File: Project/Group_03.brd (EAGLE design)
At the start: 56.4 x 71.1 mm, 29 parts, among them J1 POWER_JACKPTH_LOCK, U1 +12v, U3 TCA9546APW, U4 TMUX1208RSV

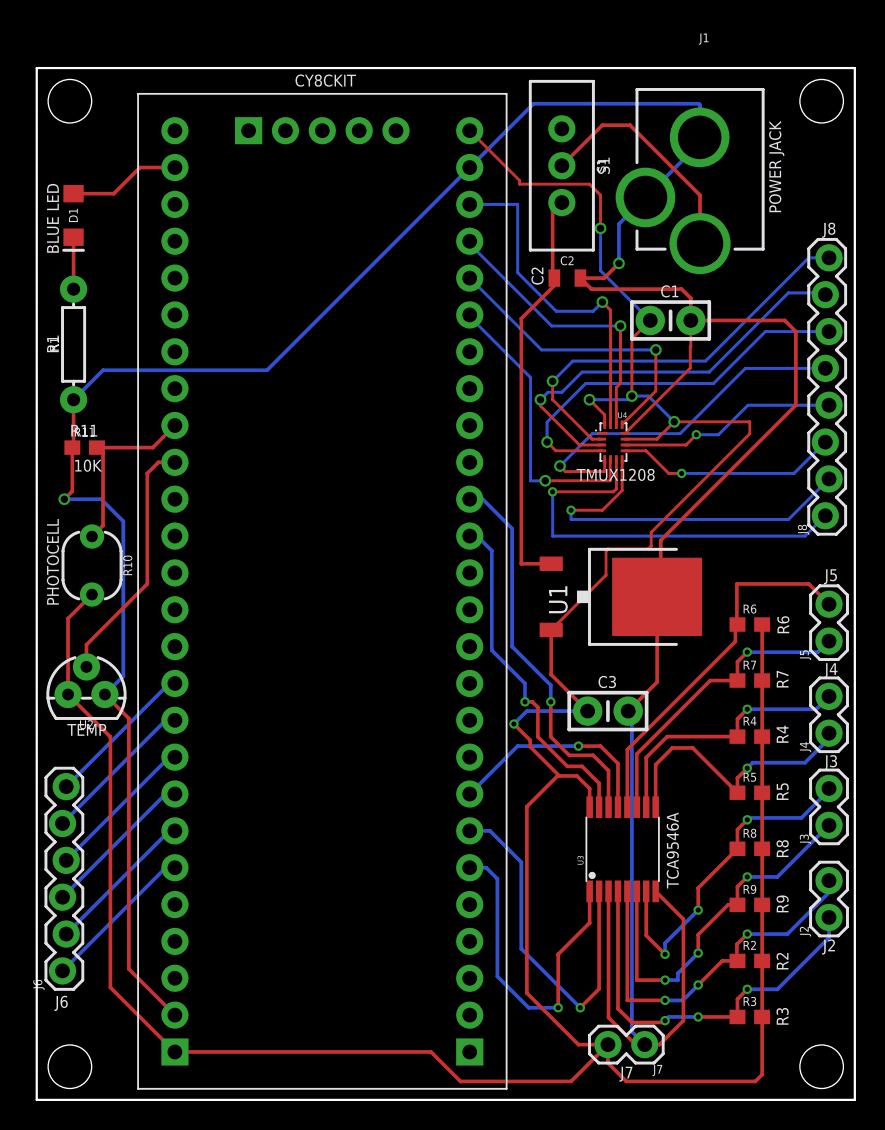
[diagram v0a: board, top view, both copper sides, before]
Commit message: Change silkscreen line width in Library for MUX, TCA and CY8
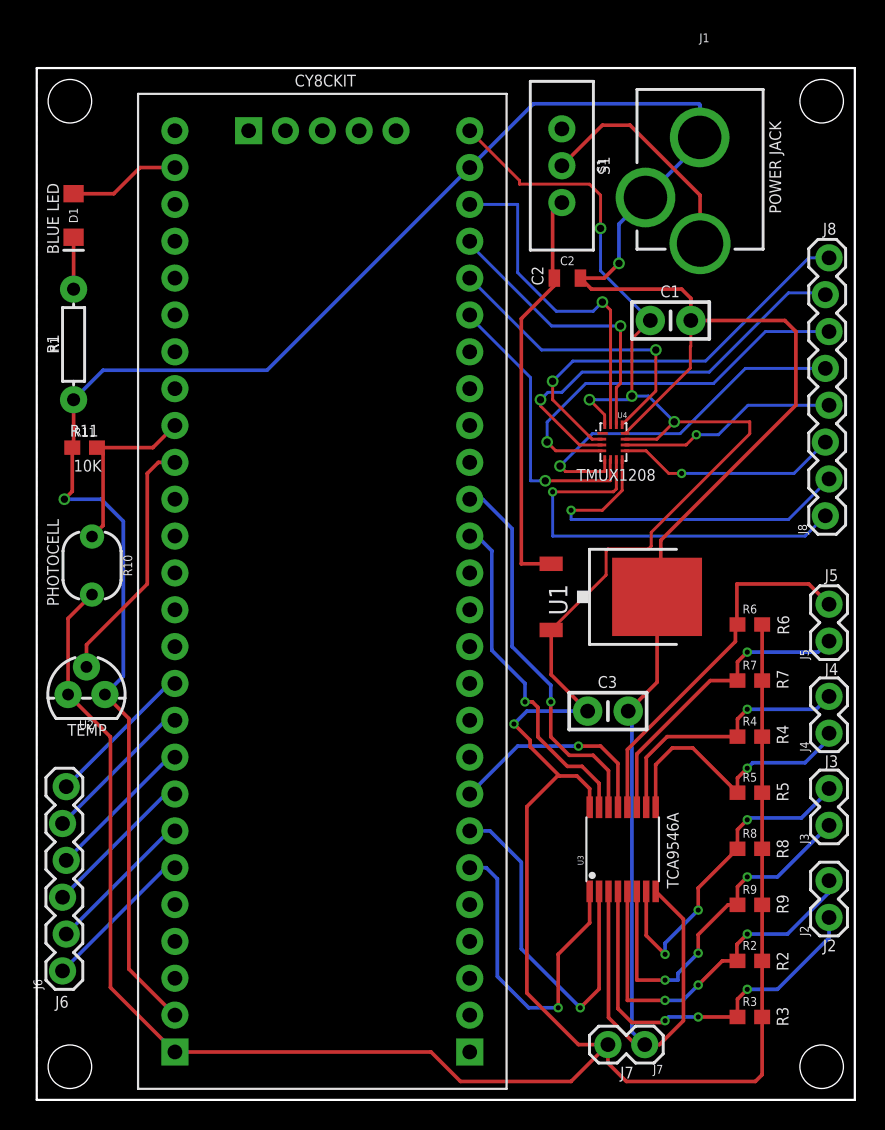
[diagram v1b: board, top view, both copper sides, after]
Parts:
- U$1: device CY8KIT-059:CY8CKIT-059_TARGET -> Group_03_Library:CY8CKIT-059_TARGET
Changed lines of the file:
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@@
 <layers>
 <layer number="1" name="Top" color="4" fill="1" visible="yes" active="yes"/>
-<layer number="16" name="Bottom" color="1" fill="1" visible="yes" active="yes"/>
-<layer number="17" name="Pads" color="2" fill="1" visible="yes" active="yes"/>
-<layer number="18" name="Vias" color="2" fill="1" visible="yes" active="yes"/>
-<layer number="19" name="Unrouted" color="6" fill="1" visible="yes" active="yes"/>
-<layer number="20" name="Dimension" color="61" fill="1" visible="yes" active="yes"/>
+<layer number="16" name="Bottom" color="1" fill="1" visible="no" active="yes"/>
+<layer number="17" name="Pads" color="2" fill="1" visible="no" active="yes"/>
+<layer number="18" name="Vias" color="2" fill="1" visible="no" active="yes"/>
+<layer number="19" name="Unrouted" color="6" fill="1" visible="no" active="yes"/>
+<layer number="20" name="Dimension" color="61" fill="1" visible="no" active="yes"/>
 <layer number="21" name="tPlace" color="13" fill="1" visible="yes" active="yes"/>
-<layer number="22" name="bPlace" color="7" fill="1" visible="yes" active="yes"/>
-<layer number="23" name="tOrigins" color="15" fill="1" visible="yes" active="yes"/>
-<layer number="24" name="bOrigins" color="15" fill="1" visible="yes" active="yes"/>
-<layer number="25" name="tNames" color="7" fill="1" visible="yes" active="yes"/>
-<layer number="26" name="bNames" color="7" fill="1" visible="yes" active="yes"/>
-<layer number="27" name="tValues" color="7" fill="1" visible="yes" active="yes"/>
-<layer number="28" name="bValues" color="7" fill="1" visible="yes" active="yes"/>
+<layer number="22" name="bPlace" color="7" fill="1" visible="no" active="yes"/>
+<layer number="23" name="tOrigins" color="15" fill="1" visible="no" active="yes"/>
+<layer number="24" name="bOrigins" color="15" fill="1" visible="no" active="yes"/>
+<layer number="25" name="tNames" color="7" fill="1" visible="no" active="yes"/>
+<layer number="26" name="bNames" color="7" fill="1" visible="no" active="yes"/>
+<layer number="27" name="tValues" color="7" fill="1" visible="no" active="yes"/>
+<layer number="28" name="bValues" color="7" fill="1" visible="no" active="yes"/>
 <layer number="29" name="tStop" color="7" fill="3" visible="no" active="yes"/>
 <layer number="30" name="bStop" color="7" fill="6" visible="no" active="yes"/>
@@
 <layer number="33" name="tFinish" color="6" fill="3" visible="no" active="yes"/>
 <layer number="34" name="bFinish" color="6" fill="6" visible="no" active="yes"/>
-<layer number="35" name="tGlue" color="7" fill="4" visible="yes" active="yes"/>
+<layer number="35" name="tGlue" color="7" fill="4" visible="no" active="yes"/>
 <layer number="36" name="bGlue" color="7" fill="5" visible="no" active="yes"/>
-<layer number="37" name="tTest" color="7" fill="1" visible="yes" active="yes"/>
-<layer number="38" name="bTest" color="7" fill="1" visible="yes" active="yes"/>
-<layer number="39" name="tKeepout" color="4" fill="11" visible="yes" active="yes"/>
-<layer number="40" name="bKeepout" color="1" fill="11" visible="yes" active="yes"/>
+<layer number="37" name="tTest" color="7" fill="1" visible="no" active="yes"/>
+<layer number="38" name="bTest" color="7" fill="1" visible="no" active="yes"/>
+<layer number="39" name="tKeepout" color="4" fill="11" visible="no" active="yes"/>
+<layer number="40" name="bKeepout" color="1" fill="11" visible="no" active="yes"/>
 <layer number="41" name="tRestrict" color="4" fill="10" visible="no" active="yes"/>
 <layer number="42" name="bRestrict" color="1" fill="10" visible="no" active="yes"/>
 <layer number="43" name="vRestrict" color="2" fill="10" visible="no" active="yes"/>
 <layer number="44" name="Drills" color="7" fill="1" visible="no" active="yes"/>
-<layer number="45" name="Holes" color="63" fill="1" visible="yes" active="yes"/>
+<layer number="45" name="Holes" color="63" fill="1" visible="no" active="yes"/>
 <layer number="46" name="Milling" color="3" fill="1" visible="no" active="yes"/>
 <layer number="47" name="Measures" color="7" fill="1" visible="no" active="yes"/>
-<layer number="48" name="Document" color="7" fill="1" visible="yes" active="yes"/>
-<layer number="49" name="Reference" color="7" fill="1" visible="yes" active="yes"/>
+<layer number="48" name="Document" color="7" fill="1" visible="no" active="yes"/>
+<layer number="49" name="Reference" color="7" fill="1" visible="no" active="yes"/>
 <layer number="50" name="dxf" color="7" fill="1" visible="no" active="no"/>
-<layer number="51" name="tDocu" color="7" fill="1" visible="yes" active="yes"/>
-<layer number="52" name="bDocu" color="7" fill="1" visible="yes" active="yes"/>
+<layer number="51" name="tDocu" color="7" fill="1" visible="no" active="yes"/>
+<layer number="52" name="bDocu" color="7" fill="1" visible="no" active="yes"/>
 <layer number="53" name="tGND_GNDA" color="7" fill="9" visible="no" active="no"/>
 <layer number="54" name="bGND_GNDA" color="1" fill="9" visible="no" active="no"/>
@@
 <attribute name="VALUE" x="33.782" y="64.389" size="0.6096" layer="27" font="vector" ratio="20" rot="R270" align="top-center"/>
 </element>
-<element name="U$1" library="CY8KIT-059" package="CY8CKIT-059_TARGET" value="CY8CKIT-059_TARGET" x="20.955" y="33.782" smashed="yes" rot="R270"/>
+<element name="U$1" library="Group_03_Library" package="CY8CKIT-059_TARGET" value="CY8CKIT-059_TARGET" x="20.955" y="33.782" smashed="yes" rot="R270"/>
 <element name="U1" library="SparkFun-IC-Power" package="TO-252" value="+12v" x="40.259" y="34.671" smashed="yes" rot="R270">
 <attribute name="NAME" x="36.576" y="33.401" size="1.27" layer="25" rot="R90"/>

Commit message: Last modifications to schematic, board and check rules
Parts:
- R1: value (none) -> 330
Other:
- board text added: "CY8CKIT-059"
- board text removed: "CY8CKIT"

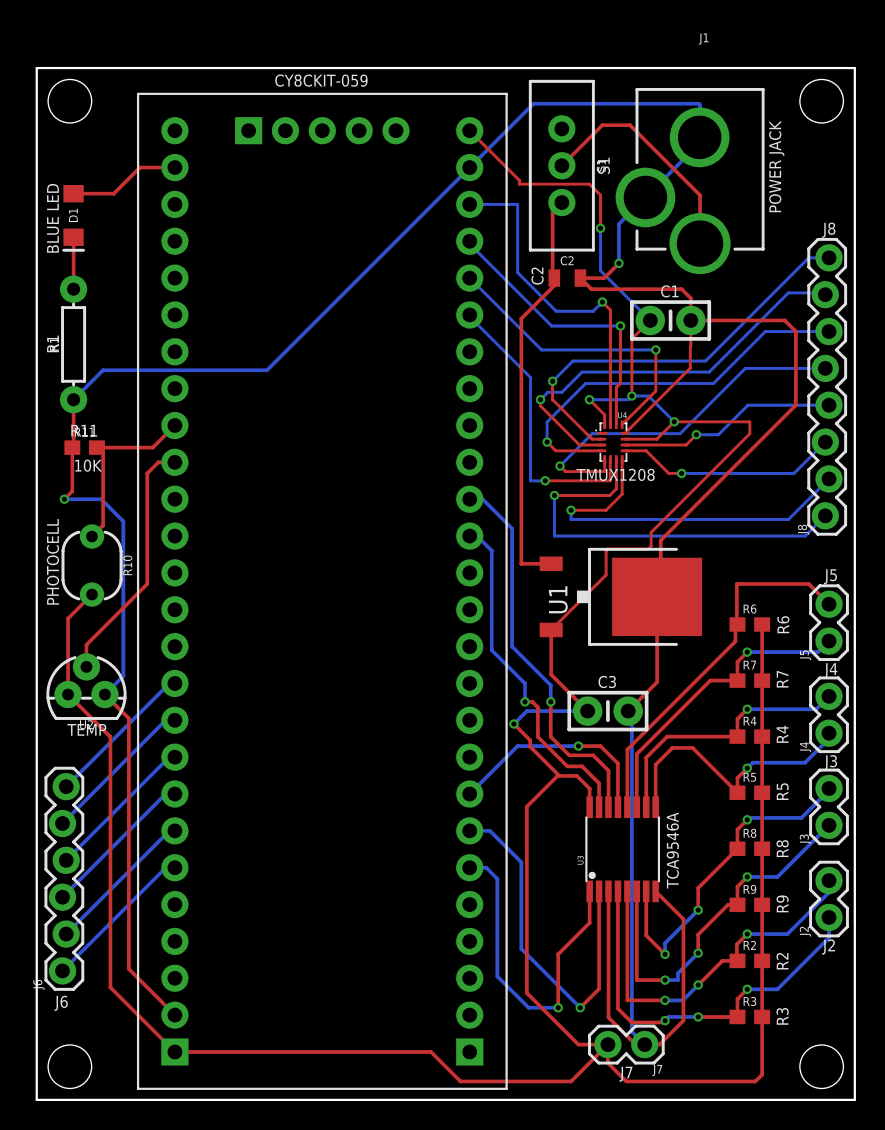
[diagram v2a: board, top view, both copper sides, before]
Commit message: Silscreen SMD components
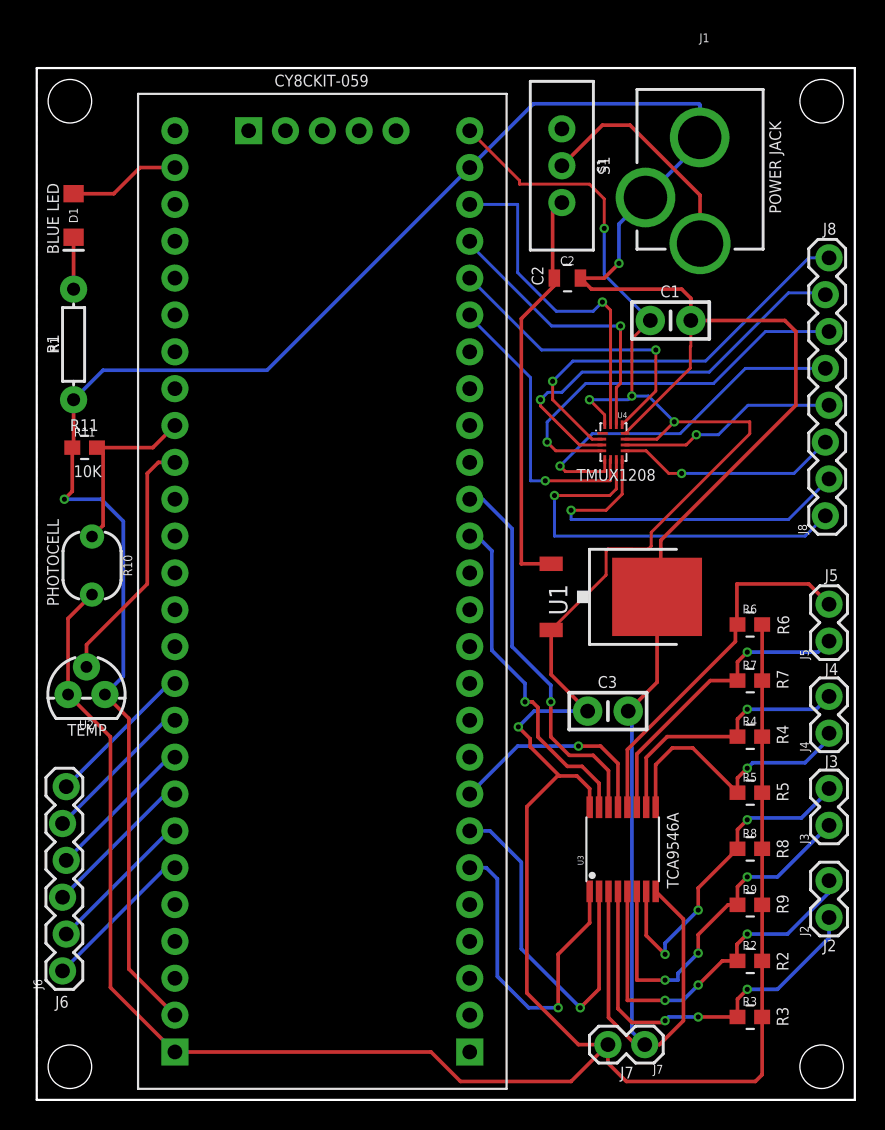
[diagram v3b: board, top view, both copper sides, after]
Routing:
- net 5V: track 220.7 -> 220.2 mm
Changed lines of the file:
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@@
 <setting verticaltext="up"/>
 </settings>
-<grid distance="50" unitdist="mil" unit="mil" style="lines" multiple="1" display="yes" altdistance="5" altunitdist="mil" altunit="mm"/>
+<grid distance="50" unitdist="mil" unit="mil" style="lines" multiple="1" display="yes" altdistance="0.05" altunitdist="mm" altunit="mm"/>
 <layers>
 <layer number="1" name="Top" color="4" fill="1" visible="yes" active="yes"/>
@@
 <layer number="27" name="tValues" color="7" fill="1" visible="yes" active="yes"/>
 <layer number="28" name="bValues" color="7" fill="1" visible="yes" active="yes"/>
-<layer number="29" name="tStop" color="7" fill="3" visible="no" active="yes"/>
+<layer number="29" name="tStop" color="7" fill="3" visible="yes" active="yes"/>
 <layer number="30" name="bStop" color="7" fill="6" visible="no" active="yes"/>
 <layer number="31" name="tCream" color="7" fill="4" visible="no" active="yes"/>
@@
 <layer number="45" name="Holes" color="63" fill="1" visible="yes" active="yes"/>
 <layer number="46" name="Milling" color="3" fill="1" visible="no" active="yes"/>
-<layer number="47" name="Measures" color="7" fill="1" visible="no" active="yes"/>
+<layer number="47" name="Measures" color="7" fill="1" visible="yes" active="yes"/>
 <layer number="48" name="Document" color="7" fill="1" visible="yes" active="yes"/>
 <layer number="49" name="Reference" color="7" fill="1" visible="yes" active="yes"/>
@@
 <text x="1.524" y="58.293" size="0.8128" layer="21" font="vector" ratio="24" rot="R90">BLUE LED</text>
 <text x="1.524" y="51.435" size="0.8128" layer="21" font="vector" ratio="24" rot="R90">R1</text>
-<text x="2.54" y="43.307" size="0.8128" layer="21" font="vector" ratio="15">10K</text>
-<text x="2.286" y="45.72" size="0.8128" layer="21" font="vector" ratio="24">R11</text>
+<text x="2.54" y="42.926" size="0.8128" layer="21" font="vector" ratio="24">10K</text>
+<text x="2.286" y="46.101" size="0.8128" layer="21" font="vector" ratio="24">R11</text>
 <text x="1.524" y="34.036" size="0.8128" layer="21" font="vector" ratio="24" rot="R90">PHOTOCELL</text>
 <text x="4.826" y="25.908" size="0.8128" layer="21" font="vector" ratio="24" rot="R180">TEMP</text>
@@
 <text x="37.211" y="42.672" size="0.8128" layer="21" font="vector" ratio="24">TMUX1208</text>
 <text x="16.383" y="69.85" size="0.8128" layer="21" font="vector" ratio="24">CY8CKIT-059</text>
+<wire x1="3.048" y1="45.77" x2="3.556" y2="45.77" width="0.1524" layer="21"/>
+<wire x1="3.048" y1="44.173" x2="3.556" y2="44.173" width="0.1524" layer="21"/>
+<wire x1="48.895" y1="33.601" x2="49.403" y2="33.601" width="0.1524" layer="21"/>
+<wire x1="48.915" y1="31.931" x2="49.423" y2="31.931" width="0.1524" layer="21"/>
+<wire x1="48.905" y1="29.711" x2="49.413" y2="29.711" width="0.1524" layer="21"/>
+<wire x1="48.925" y1="28.091" x2="49.433" y2="28.091" width="0.1524" layer="21"/>
+<wire x1="48.905" y1="25.861" x2="49.413" y2="25.861" width="0.1524" layer="21"/>
+<wire x1="48.925" y1="24.191" x2="49.433" y2="24.191" width="0.1524" layer="21"/>
+<wire x1="48.905" y1="22.011" x2="49.413" y2="22.011" width="0.1524" layer="21"/>
+<wire x1="48.925" y1="20.341" x2="49.433" y2="20.341" width="0.1524" layer="21"/>
+<wire x1="48.905" y1="18.111" x2="49.413" y2="18.111" width="0.1524" layer="21"/>
+<wire x1="48.925" y1="16.491" x2="49.433" y2="16.491" width="0.1524" layer="21"/>
+<wire x1="48.905" y1="14.261" x2="49.413" y2="14.261" width="0.1524" layer="21"/>
+<wire x1="48.925" y1="12.641" x2="49.433" y2="12.641" width="0.1524" layer="21"/>
+<wire x1="48.905" y1="10.411" x2="49.413" y2="10.411" width="0.1524" layer="21"/>
+<wire x1="48.925" y1="8.741" x2="49.433" y2="8.741" width="0.1524" layer="21"/>
+<wire x1="48.905" y1="6.511" x2="49.413" y2="6.511" width="0.1524" layer="21"/>
+<wire x1="48.925" y1="4.891" x2="49.433" y2="4.891" width="0.1524" layer="21"/>
+<wire x1="36.315" y1="57.551" x2="36.823" y2="57.551" width="0.1524" layer="21"/>
+<wire x1="36.335" y1="55.731" x2="36.843" y2="55.731" width="0.1524" layer="21"/>
 </plain>
 <attributes>
@@
 <wire x1="33.274" y1="63.373" x2="33.274" y2="63.119" width="0.2032" layer="1"/>
 <wire x1="33.274" y1="63.119" x2="38.1" y2="63.119" width="0.2032" layer="1"/>
-<wire x1="38.1" y1="63.119" x2="38.862" y2="62.357" width="0.2032" layer="1"/>
-<wire x1="38.862" y1="62.357" x2="38.862" y2="60.071" width="0.2032" layer="1"/>
-<via x="38.862" y="60.071" extent="1-16" drill="0.35"/>
-<wire x1="38.862" y1="57.15" x2="42.291" y2="53.721" width="0.2032" layer="16"/>
-<wire x1="38.862" y1="60.071" x2="38.862" y2="57.15" width="0.2032" layer="16"/>
+<wire x1="38.1" y1="63.119" x2="39.116" y2="62.103" width="0.2032" layer="1"/>
+<wire x1="39.116" y1="62.103" x2="39.116" y2="60.071" width="0.2032" layer="1"/>
+<via x="39.116" y="60.071" extent="1-16" drill="0.35"/>
+<wire x1="39.116" y1="56.896" x2="42.291" y2="53.721" width="0.2032" layer="16"/>
+<wire x1="39.116" y1="60.071" x2="39.116" y2="56.896" width="0.2032" layer="16"/>
 <wire x1="42.291" y1="53.721" x2="41.021" y2="52.451" width="0.2032" layer="1"/>
 <wire x1="41.021" y1="52.451" x2="41.021" y2="48.514" width="0.2032" layer="1"/>
@@
 <wire x1="42.3526" y1="39.1173375" x2="49.149" y2="45.9137375" width="0.2032" layer="1"/>
 <wire x1="49.149" y1="46.736" x2="43.942" y2="46.736" width="0.2032" layer="1"/>
-<via x="32.893" y="25.908" extent="1-16" drill="0.35"/>
-<wire x1="32.893" y1="25.908" x2="33.782" y2="26.797" width="0.254" layer="16"/>
-<wire x1="33.782" y1="26.797" x2="37.973" y2="26.797" width="0.254" layer="16"/>
+<via x="33.193" y="25.708" extent="1-16" drill="0.35"/>
+<wire x1="33.193" y1="25.708" x2="34.282" y2="26.797" width="0.254" layer="16"/>
+<wire x1="34.282" y1="26.797" x2="37.973" y2="26.797" width="0.254" layer="16"/>
 <contactref element="R2" pad="2"/>
 <contactref element="R7" pad="2"/>
@@
 <wire x1="36.0266625" y1="22.3266" x2="35.8996625" y2="22.3266" width="0.254" layer="1"/>
 <wire x1="36.0266625" y1="22.3266" x2="34.0106" y2="24.3426625" width="0.254" layer="1"/>
-<wire x1="34.0106" y1="24.3426625" x2="34.0106" y2="24.7904" width="0.254" layer="1"/>
-<wire x1="34.0106" y1="24.7904" x2="32.893" y2="25.908" width="0.254" layer="1"/>
+<wire x1="34.0106" y1="24.3426625" x2="34.0106" y2="24.8904" width="0.254" layer="1"/>
+<wire x1="34.0106" y1="24.8904" x2="33.193" y2="25.708" width="0.254" layer="1"/>
 <wire x1="38.111" y1="21.452" x2="37.2364" y2="22.3266" width="0.254" layer="1"/>
 <wire x1="39.37" y1="3.81" x2="37.338" y2="3.81" width="0.254" layer="1"/>
